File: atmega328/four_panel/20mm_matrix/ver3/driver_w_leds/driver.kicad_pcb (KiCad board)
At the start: 2 copper layers, 40 x 40 mm, 308 parts, among them IC1 ATMEGA328P-M, IC2 ATMEGA328P-M, IC3 ATMEGA328P-M, IC4 ATMEGA328P-M, P1 CONN_2X2, P2 CONN_2X2, P3 CONN_2X2, P4 CONN_2X2, X1 CER_RESO, X2 CER_RESO, X3 CER_RESO, X4 CER_RESO

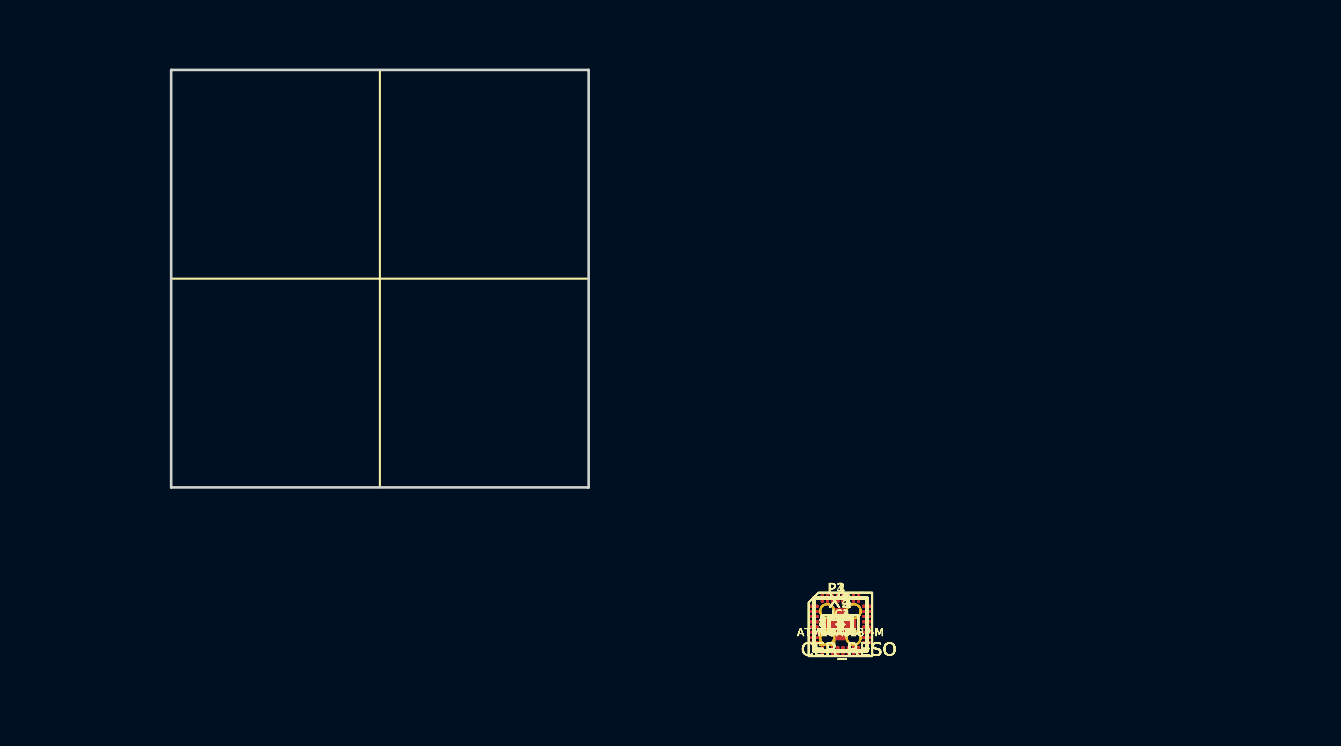
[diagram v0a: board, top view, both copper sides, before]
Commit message: Added footprint for 2x2 SMD header. Did preliminary fit test - OK but might step resistors and capacitors down to 0402 to make routing easier.
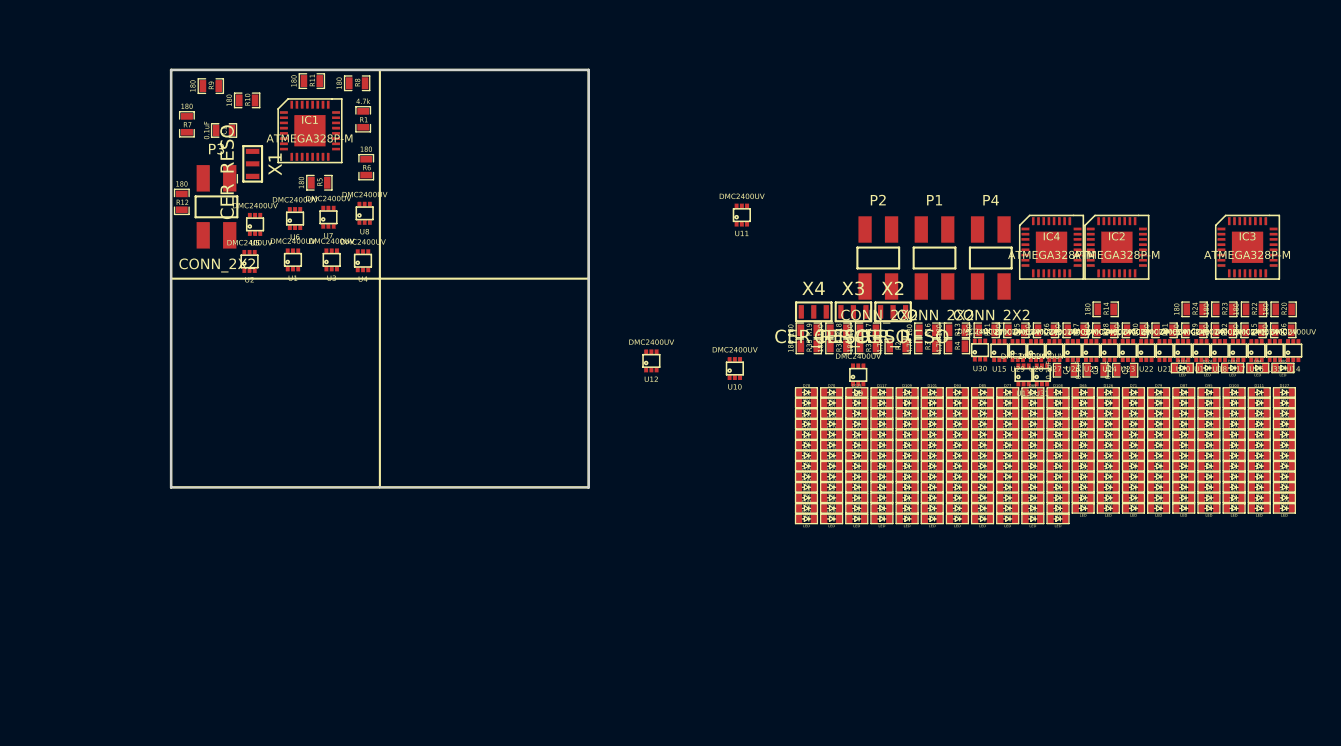
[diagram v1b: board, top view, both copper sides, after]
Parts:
- added U1: DMC2400UV, DMC2400UV, F.Cu at (61.7, 68.2)
- added U10: DMC2400UV, DMC2400UV, F.Cu at (104.0, 78.6)
- added U11: DMC2400UV, DMC2400UV, F.Cu at (104.7, 63.9)
- added U12: DMC2400UV, DMC2400UV, F.Cu at (96.0, 77.9)
- added U13: DMC2400UV, DMC2400UV, F.Cu at (131.7, 79.2)
- added U14: DMC2400UV, DMC2400UV, F.Cu at (157.5, 76.9)
- added U15: DMC2400UV, DMC2400UV, F.Cu at (129.3, 76.9)
- added U16: DMC2400UV, DMC2400UV, F.Cu at (154.0, 76.9)
- added U17: DMC2400UV, DMC2400UV, F.Cu at (152.2, 76.9)
- added U18: DMC2400UV, DMC2400UV, F.Cu at (150.5, 76.9)
- added U19: DMC2400UV, DMC2400UV, F.Cu at (148.7, 76.9)
- added U2: DMC2400UV, DMC2400UV, F.Cu at (57.5, 68.3)
- added U20: DMC2400UV, DMC2400UV, F.Cu at (146.9, 76.9)
- added U21: DMC2400UV, DMC2400UV, F.Cu at (145.2, 76.9)
- added U22: DMC2400UV, DMC2400UV, F.Cu at (143.4, 76.9)
- added U23: DMC2400UV, DMC2400UV, F.Cu at (141.7, 76.9)
- added U24: DMC2400UV, DMC2400UV, F.Cu at (139.9, 76.9)
- added U25: DMC2400UV, DMC2400UV, F.Cu at (138.2, 76.9)
- added U26: DMC2400UV, DMC2400UV, F.Cu at (136.4, 76.9)
- added U27: DMC2400UV, DMC2400UV, F.Cu at (134.6, 76.9)
- added U28: DMC2400UV, DMC2400UV, F.Cu at (132.9, 76.9)
- added U29: DMC2400UV, DMC2400UV, F.Cu at (131.1, 76.9)
- added U3: DMC2400UV, DMC2400UV, F.Cu at (65.4, 68.2)
- added U30: DMC2400UV, DMC2400UV, F.Cu at (127.5, 76.8)
- added U31: DMC2400UV, DMC2400UV, F.Cu at (133.4, 79.2)
- added U32: DMC2400UV, DMC2400UV, F.Cu at (155.8, 76.9)
- added U4: DMC2400UV, DMC2400UV, F.Cu at (68.4, 68.3)
- added U5: DMC2400UV, DMC2400UV, F.Cu at (58.0, 64.8)
- added U6: DMC2400UV, DMC2400UV, F.Cu at (61.9, 64.2)
- added U7: DMC2400UV, DMC2400UV, F.Cu at (65.1, 64.1)
- added U8: DMC2400UV, DMC2400UV, F.Cu at (68.5, 63.7)
- added U9: DMC2400UV, DMC2400UV, F.Cu at (115.8, 79.2)
- P1, P2, P3, P4: footprint PIN_ARRAY_2X2 -> SMD_2X2
- moved R9 79.4 mm to (53.8, 51.5)
- moved R7 78.8 mm to (51.5, 55.2), turned to 270 degrees
- moved R10 75.8 mm to (57.3, 52.9)
- moved C1 75.7 mm to (55.1, 55.8)
- moved R12 75.0 mm to (51.0, 62.6), turned to 270 degrees
- moved R11 72.6 mm to (63.5, 51.1)
- moved P3 71.9 mm to (54.3, 63.1)
- moved X1 71.5 mm to (57.8, 59.0), turned to 270 degrees
- moved R8 69.5 mm to (67.8, 51.3)
- moved IC1 69.4 mm to (63.3, 55.8)
- moved R1 66.6 mm to (68.4, 54.7), turned to 270 degrees
- moved R5 65.4 mm to (64.2, 60.8)
- moved R6 63.1 mm to (68.7, 59.3), turned to 270 degrees
- moved IC3 53.2 mm to (153.1, 67.0)
- moved R20 52.1 mm to (156.6, 72.9)
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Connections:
- D1 pad 2: /ROW0_DRV0 -> /ROW0_INV0
- D10 pad 2: /ROW1_DRV0 -> /ROW1_INV0
- D100 pad 2: /ROW3_DRV1 -> /ROW3_INV1
- D101 pad 2: /ROW4_DRV1 -> /ROW4_INV1
- D102 pad 2: /ROW5_DRV1 -> /ROW5_INV1
- D103 pad 2: /ROW6_DRV1 -> /ROW6_INV1
- D104 pad 2: /ROW7_DRV1 -> /ROW7_INV1
- D105 pad 2: /ROW0_DRV1 -> /ROW0_INV1
- D106 pad 2: /ROW1_DRV1 -> /ROW1_INV1
- D107 pad 2: /ROW2_DRV1 -> /ROW2_INV1
- D108 pad 2: /ROW3_DRV1 -> /ROW3_INV1
- D109 pad 2: /ROW4_DRV1 -> /ROW4_INV1
- D11 pad 2: /ROW2_DRV0 -> /ROW2_INV0
- D110 pad 2: /ROW5_DRV1 -> /ROW5_INV1
- D111 pad 2: /ROW6_DRV1 -> /ROW6_INV1
- D112 pad 2: /ROW7_DRV1 -> /ROW7_INV1
- D113 pad 2: /ROW0_DRV1 -> /ROW0_INV1
- D114 pad 2: /ROW1_DRV1 -> /ROW1_INV1
- D115 pad 2: /ROW2_DRV1 -> /ROW2_INV1
- D116 pad 2: /ROW3_DRV1 -> /ROW3_INV1
- D117 pad 2: /ROW4_DRV1 -> /ROW4_INV1
- D118 pad 2: /ROW5_DRV1 -> /ROW5_INV1
- D119 pad 2: /ROW6_DRV1 -> /ROW6_INV1
- D12 pad 2: /ROW3_DRV0 -> /ROW3_INV0
- D120 pad 2: /ROW7_DRV1 -> /ROW7_INV1
- D121 pad 2: /ROW0_DRV1 -> /ROW0_INV1
- D122 pad 2: /ROW1_DRV1 -> /ROW1_INV1
- D123 pad 2: /ROW2_DRV1 -> /ROW2_INV1
- D124 pad 2: /ROW3_DRV1 -> /ROW3_INV1
- D125 pad 2: /ROW4_DRV1 -> /ROW4_INV1
- D126 pad 2: /ROW5_DRV1 -> /ROW5_INV1
- D127 pad 2: /ROW6_DRV1 -> /ROW6_INV1
- D128 pad 2: /ROW7_DRV1 -> /ROW7_INV1
- D129 pad 2: /ROW0_DRV2 -> /ROW0_INV2
- D13 pad 2: /ROW4_DRV0 -> /ROW4_INV0
- D130 pad 2: /ROW1_DRV2 -> /ROW1_INV2
- D131 pad 2: /ROW2_DRV2 -> /ROW2_INV2
- D132 pad 2: /ROW3_DRV2 -> /ROW3_INV2
- D133 pad 2: /ROW4_DRV2 -> /ROW4_INV2
- D134 pad 2: /ROW5_DRV2 -> /ROW5_INV2
- D135 pad 2: /ROW6_DRV2 -> /ROW6_INV2
- D136 pad 2: /ROW7_DRV2 -> /ROW7_INV2
- D137 pad 2: /ROW0_DRV2 -> /ROW0_INV2
- D138 pad 2: /ROW1_DRV2 -> /ROW1_INV2
- D139 pad 2: /ROW2_DRV2 -> /ROW2_INV2
- D14 pad 2: /ROW5_DRV0 -> /ROW5_INV0
- D140 pad 2: /ROW3_DRV2 -> /ROW3_INV2
- D141 pad 2: /ROW4_DRV2 -> /ROW4_INV2
- D142 pad 2: /ROW5_DRV2 -> /ROW5_INV2
- D143 pad 2: /ROW6_DRV2 -> /ROW6_INV2
- D144 pad 2: /ROW7_DRV2 -> /ROW7_INV2
- D145 pad 2: /ROW0_DRV2 -> /ROW0_INV2
- D146 pad 2: /ROW1_DRV2 -> /ROW1_INV2
- D147 pad 2: /ROW2_DRV2 -> /ROW2_INV2
- D148 pad 2: /ROW3_DRV2 -> /ROW3_INV2
- D149 pad 2: /ROW4_DRV2 -> /ROW4_INV2
- D15 pad 2: /ROW6_DRV0 -> /ROW6_INV0
- D150 pad 2: /ROW5_DRV2 -> /ROW5_INV2
- D151 pad 2: /ROW6_DRV2 -> /ROW6_INV2
- D152 pad 2: /ROW7_DRV2 -> /ROW7_INV2
- D153 pad 2: /ROW0_DRV2 -> /ROW0_INV2
- D154 pad 2: /ROW1_DRV2 -> /ROW1_INV2
- D155 pad 2: /ROW2_DRV2 -> /ROW2_INV2
- D156 pad 2: /ROW3_DRV2 -> /ROW3_INV2
- D157 pad 2: /ROW4_DRV2 -> /ROW4_INV2
- D158 pad 2: /ROW5_DRV2 -> /ROW5_INV2
- D159 pad 2: /ROW6_DRV2 -> /ROW6_INV2
- D16 pad 2: /ROW7_DRV0 -> /ROW7_INV0
- D160 pad 2: /ROW7_DRV2 -> /ROW7_INV2
- D161 pad 2: /ROW0_DRV2 -> /ROW0_INV2
- D162 pad 2: /ROW1_DRV2 -> /ROW1_INV2
- D163 pad 2: /ROW2_DRV2 -> /ROW2_INV2
- D164 pad 2: /ROW3_DRV2 -> /ROW3_INV2
- D165 pad 2: /ROW4_DRV2 -> /ROW4_INV2
- D166 pad 2: /ROW5_DRV2 -> /ROW5_INV2
- D167 pad 2: /ROW6_DRV2 -> /ROW6_INV2
- D168 pad 2: /ROW7_DRV2 -> /ROW7_INV2
- D169 pad 2: /ROW0_DRV2 -> /ROW0_INV2
- D17 pad 2: /ROW0_DRV0 -> /ROW0_INV0
- D170 pad 2: /ROW1_DRV2 -> /ROW1_INV2
- D171 pad 2: /ROW2_DRV2 -> /ROW2_INV2
- D172 pad 2: /ROW3_DRV2 -> /ROW3_INV2
- D173 pad 2: /ROW4_DRV2 -> /ROW4_INV2
- D174 pad 2: /ROW5_DRV2 -> /ROW5_INV2
- D175 pad 2: /ROW6_DRV2 -> /ROW6_INV2
- D176 pad 2: /ROW7_DRV2 -> /ROW7_INV2
- D177 pad 2: /ROW0_DRV2 -> /ROW0_INV2
- D178 pad 2: /ROW1_DRV2 -> /ROW1_INV2
- D179 pad 2: /ROW2_DRV2 -> /ROW2_INV2
- D18 pad 2: /ROW1_DRV0 -> /ROW1_INV0
- D180 pad 2: /ROW3_DRV2 -> /ROW3_INV2
- D181 pad 2: /ROW4_DRV2 -> /ROW4_INV2
- D182 pad 2: /ROW5_DRV2 -> /ROW5_INV2
- D183 pad 2: /ROW6_DRV2 -> /ROW6_INV2
- D184 pad 2: /ROW7_DRV2 -> /ROW7_INV2
- D185 pad 2: /ROW0_DRV2 -> /ROW0_INV2
- D186 pad 2: /ROW1_DRV2 -> /ROW1_INV2
- D187 pad 2: /ROW2_DRV2 -> /ROW2_INV2
- D188 pad 2: /ROW3_DRV2 -> /ROW3_INV2
- D189 pad 2: /ROW4_DRV2 -> /ROW4_INV2
- D19 pad 2: /ROW2_DRV0 -> /ROW2_INV0
- D190 pad 2: /ROW5_DRV2 -> /ROW5_INV2
- D191 pad 2: /ROW6_DRV2 -> /ROW6_INV2
- D192 pad 2: /ROW7_DRV2 -> /ROW7_INV2
- D193 pad 2: /ROW0_DRV3 -> /ROW0_INV3
- D194 pad 2: /ROW1_DRV3 -> /ROW1_INV3
- D195 pad 2: /ROW2_DRV3 -> /ROW2_INV3
- D196 pad 2: /ROW3_DRV3 -> /ROW3_INV3
- D197 pad 2: /ROW4_DRV3 -> /ROW4_INV3
- D198 pad 2: /ROW5_DRV3 -> /ROW5_INV3
- D199 pad 2: /ROW6_DRV3 -> /ROW6_INV3
- D2 pad 2: /ROW1_DRV0 -> /ROW1_INV0
- D20 pad 2: /ROW3_DRV0 -> /ROW3_INV0
- D200 pad 2: /ROW7_DRV3 -> /ROW7_INV3
- D201 pad 2: /ROW0_DRV3 -> /ROW0_INV3
- D202 pad 2: /ROW1_DRV3 -> /ROW1_INV3
- D203 pad 2: /ROW2_DRV3 -> /ROW2_INV3
- D204 pad 2: /ROW3_DRV3 -> /ROW3_INV3
- D205 pad 2: /ROW4_DRV3 -> /ROW4_INV3
- D206 pad 2: /ROW5_DRV3 -> /ROW5_INV3
- D207 pad 2: /ROW6_DRV3 -> /ROW6_INV3
- D208 pad 2: /ROW7_DRV3 -> /ROW7_INV3
- D209 pad 2: /ROW0_DRV3 -> /ROW0_INV3
- D21 pad 2: /ROW4_DRV0 -> /ROW4_INV0
- D210 pad 2: /ROW1_DRV3 -> /ROW1_INV3
- D211 pad 2: /ROW2_DRV3 -> /ROW2_INV3
- D212 pad 2: /ROW3_DRV3 -> /ROW3_INV3
- D213 pad 2: /ROW4_DRV3 -> /ROW4_INV3
- D214 pad 2: /ROW5_DRV3 -> /ROW5_INV3
- D215 pad 2: /ROW6_DRV3 -> /ROW6_INV3
- D216 pad 2: /ROW7_DRV3 -> /ROW7_INV3
- D217 pad 2: /ROW0_DRV3 -> /ROW0_INV3
- D218 pad 2: /ROW1_DRV3 -> /ROW1_INV3
- D219 pad 2: /ROW2_DRV3 -> /ROW2_INV3
- D22 pad 2: /ROW5_DRV0 -> /ROW5_INV0
- D220 pad 2: /ROW3_DRV3 -> /ROW3_INV3
- D221 pad 2: /ROW4_DRV3 -> /ROW4_INV3
- D222 pad 2: /ROW5_DRV3 -> /ROW5_INV3
- D223 pad 2: /ROW6_DRV3 -> /ROW6_INV3
- D224 pad 2: /ROW7_DRV3 -> /ROW7_INV3
- D225 pad 2: /ROW0_DRV3 -> /ROW0_INV3
- D226 pad 2: /ROW1_DRV3 -> /ROW1_INV3
- D227 pad 2: /ROW2_DRV3 -> /ROW2_INV3
- D228 pad 2: /ROW3_DRV3 -> /ROW3_INV3
- D229 pad 2: /ROW4_DRV3 -> /ROW4_INV3
- D23 pad 2: /ROW6_DRV0 -> /ROW6_INV0
- D230 pad 2: /ROW5_DRV3 -> /ROW5_INV3
- D231 pad 2: /ROW6_DRV3 -> /ROW6_INV3
- D232 pad 2: /ROW7_DRV3 -> /ROW7_INV3
- D233 pad 2: /ROW0_DRV3 -> /ROW0_INV3
- D234 pad 2: /ROW1_DRV3 -> /ROW1_INV3
- D235 pad 2: /ROW2_DRV3 -> /ROW2_INV3
- D236 pad 2: /ROW3_DRV3 -> /ROW3_INV3
- D237 pad 2: /ROW4_DRV3 -> /ROW4_INV3
- D238 pad 2: /ROW5_DRV3 -> /ROW5_INV3
- D239 pad 2: /ROW6_DRV3 -> /ROW6_INV3
- D24 pad 2: /ROW7_DRV0 -> /ROW7_INV0
- D240 pad 2: /ROW7_DRV3 -> /ROW7_INV3
- D241 pad 2: /ROW0_DRV3 -> /ROW0_INV3
- D242 pad 2: /ROW1_DRV3 -> /ROW1_INV3
- D243 pad 2: /ROW2_DRV3 -> /ROW2_INV3
- D244 pad 2: /ROW3_DRV3 -> /ROW3_INV3
- D245 pad 2: /ROW4_DRV3 -> /ROW4_INV3
- D246 pad 2: /ROW5_DRV3 -> /ROW5_INV3
- D247 pad 2: /ROW6_DRV3 -> /ROW6_INV3
- D248 pad 2: /ROW7_DRV3 -> /ROW7_INV3
- D249 pad 2: /ROW0_DRV3 -> /ROW0_INV3
- D25 pad 2: /ROW0_DRV0 -> /ROW0_INV0
- D250 pad 2: /ROW1_DRV3 -> /ROW1_INV3
- D251 pad 2: /ROW2_DRV3 -> /ROW2_INV3
- D252 pad 2: /ROW3_DRV3 -> /ROW3_INV3
- D253 pad 2: /ROW4_DRV3 -> /ROW4_INV3
- D254 pad 2: /ROW5_DRV3 -> /ROW5_INV3
- D255 pad 2: /ROW6_DRV3 -> /ROW6_INV3
- D256 pad 2: /ROW7_DRV3 -> /ROW7_INV3
- D26 pad 2: /ROW1_DRV0 -> /ROW1_INV0
- D27 pad 2: /ROW2_DRV0 -> /ROW2_INV0
- D28 pad 2: /ROW3_DRV0 -> /ROW3_INV0
- D29 pad 2: /ROW4_DRV0 -> /ROW4_INV0
- D3 pad 2: /ROW2_DRV0 -> /ROW2_INV0
- D30 pad 2: /ROW5_DRV0 -> /ROW5_INV0
- D31 pad 2: /ROW6_DRV0 -> /ROW6_INV0
- D32 pad 2: /ROW7_DRV0 -> /ROW7_INV0
- D33 pad 2: /ROW0_DRV0 -> /ROW0_INV0
- D34 pad 2: /ROW1_DRV0 -> /ROW1_INV0
- D35 pad 2: /ROW2_DRV0 -> /ROW2_INV0
- D36 pad 2: /ROW3_DRV0 -> /ROW3_INV0
- D37 pad 2: /ROW4_DRV0 -> /ROW4_INV0
- D38 pad 2: /ROW5_DRV0 -> /ROW5_INV0
- D39 pad 2: /ROW6_DRV0 -> /ROW6_INV0
- D4 pad 2: /ROW3_DRV0 -> /ROW3_INV0
- D40 pad 2: /ROW7_DRV0 -> /ROW7_INV0
- D41 pad 2: /ROW0_DRV0 -> /ROW0_INV0
- D42 pad 2: /ROW1_DRV0 -> /ROW1_INV0
- D43 pad 2: /ROW2_DRV0 -> /ROW2_INV0
- D44 pad 2: /ROW3_DRV0 -> /ROW3_INV0
- D45 pad 2: /ROW4_DRV0 -> /ROW4_INV0
- D46 pad 2: /ROW5_DRV0 -> /ROW5_INV0
- D47 pad 2: /ROW6_DRV0 -> /ROW6_INV0
- D48 pad 2: /ROW7_DRV0 -> /ROW7_INV0
- D49 pad 2: /ROW0_DRV0 -> /ROW0_INV0
- D5 pad 2: /ROW4_DRV0 -> /ROW4_INV0
- D50 pad 2: /ROW1_DRV0 -> /ROW1_INV0
- D51 pad 2: /ROW2_DRV0 -> /ROW2_INV0
- D52 pad 2: /ROW3_DRV0 -> /ROW3_INV0
- D53 pad 2: /ROW4_DRV0 -> /ROW4_INV0
- D54 pad 2: /ROW5_DRV0 -> /ROW5_INV0
- D55 pad 2: /ROW6_DRV0 -> /ROW6_INV0
- D56 pad 2: /ROW7_DRV0 -> /ROW7_INV0
- D57 pad 2: /ROW0_DRV0 -> /ROW0_INV0
- D58 pad 2: /ROW1_DRV0 -> /ROW1_INV0
- D59 pad 2: /ROW2_DRV0 -> /ROW2_INV0
- D6 pad 2: /ROW5_DRV0 -> /ROW5_INV0
- D60 pad 2: /ROW3_DRV0 -> /ROW3_INV0
- D61 pad 2: /ROW4_DRV0 -> /ROW4_INV0
- D62 pad 2: /ROW5_DRV0 -> /ROW5_INV0
- D63 pad 2: /ROW6_DRV0 -> /ROW6_INV0
- D64 pad 2: /ROW7_DRV0 -> /ROW7_INV0
- D65 pad 2: /ROW0_DRV1 -> /ROW0_INV1
- D66 pad 2: /ROW1_DRV1 -> /ROW1_INV1
- D67 pad 2: /ROW2_DRV1 -> /ROW2_INV1
- D68 pad 2: /ROW3_DRV1 -> /ROW3_INV1
- D69 pad 2: /ROW4_DRV1 -> /ROW4_INV1
- D7 pad 2: /ROW6_DRV0 -> /ROW6_INV0
- D70 pad 2: /ROW5_DRV1 -> /ROW5_INV1
- D71 pad 2: /ROW6_DRV1 -> /ROW6_INV1
- D72 pad 2: /ROW7_DRV1 -> /ROW7_INV1
- D73 pad 2: /ROW0_DRV1 -> /ROW0_INV1
- D74 pad 2: /ROW1_DRV1 -> /ROW1_INV1
- D75 pad 2: /ROW2_DRV1 -> /ROW2_INV1
- D76 pad 2: /ROW3_DRV1 -> /ROW3_INV1
- D77 pad 2: /ROW4_DRV1 -> /ROW4_INV1
- D78 pad 2: /ROW5_DRV1 -> /ROW5_INV1
- D79 pad 2: /ROW6_DRV1 -> /ROW6_INV1
- D8 pad 2: /ROW7_DRV0 -> /ROW7_INV0
- D80 pad 2: /ROW7_DRV1 -> /ROW7_INV1
- D81 pad 2: /ROW0_DRV1 -> /ROW0_INV1
- D82 pad 2: /ROW1_DRV1 -> /ROW1_INV1
- D83 pad 2: /ROW2_DRV1 -> /ROW2_INV1
- D84 pad 2: /ROW3_DRV1 -> /ROW3_INV1
- D85 pad 2: /ROW4_DRV1 -> /ROW4_INV1
- D86 pad 2: /ROW5_DRV1 -> /ROW5_INV1
- D87 pad 2: /ROW6_DRV1 -> /ROW6_INV1
- D88 pad 2: /ROW7_DRV1 -> /ROW7_INV1
- D89 pad 2: /ROW0_DRV1 -> /ROW0_INV1
- D9 pad 2: /ROW0_DRV0 -> /ROW0_INV0
- D90 pad 2: /ROW1_DRV1 -> /ROW1_INV1
- D91 pad 2: /ROW2_DRV1 -> /ROW2_INV1
- D92 pad 2: /ROW3_DRV1 -> /ROW3_INV1
- D93 pad 2: /ROW4_DRV1 -> /ROW4_INV1
- D94 pad 2: /ROW5_DRV1 -> /ROW5_INV1
- D95 pad 2: /ROW6_DRV1 -> /ROW6_INV1
- D96 pad 2: /ROW7_DRV1 -> /ROW7_INV1
- D97 pad 2: /ROW0_DRV1 -> /ROW0_INV1
- D98 pad 2: /ROW1_DRV1 -> /ROW1_INV1
- D99 pad 2: /ROW2_DRV1 -> /ROW2_INV1

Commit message: Finished preliminary component layout for driver with leds.
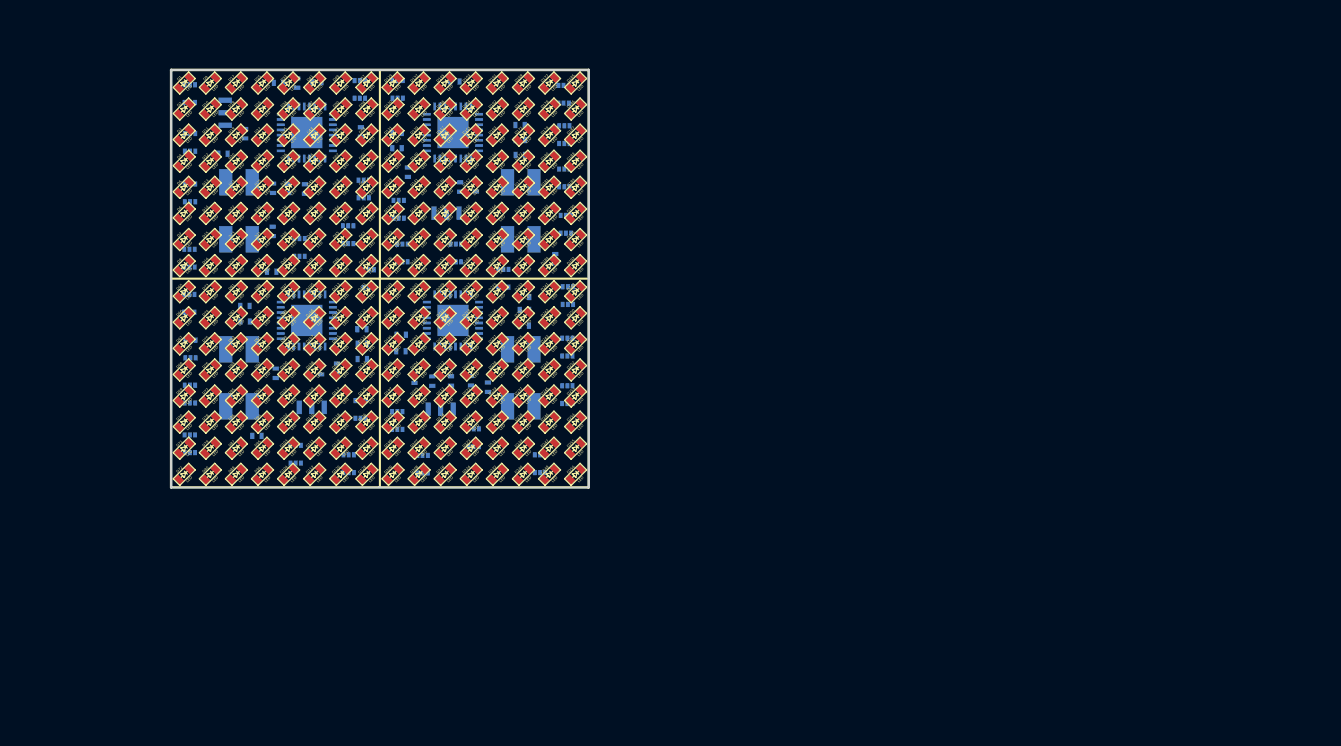
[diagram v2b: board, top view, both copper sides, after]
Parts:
- C1, C2, C3, C4: footprint SM0603_Capa -> SM0402; moved to B.Cu
- IC1, IC2, IC3, IC4, P1, P2, P3, P4, U1, U10, U11, U12, U13, U14, U15, U16, U17, U18, U19, U2, U20, U21, U22, U23, U24, U25, U26, U27, U28, U29, U3, U30, U31, U32, U4, U5, U6, U7, U8, U9, X1, X2, X3, X4: moved to B.Cu
- R1, R10, R11, R12, R13, R14, R15, R16, R17, R18, R19, R2, R20, R21, R22, R23, R24, R25, R26, R27, R28, R29, R3, R30, R31, R32, R33, R34, R35, R36, R4, R5, R6, R7, R8, R9: footprint SM0603_Resistor -> SM0402; moved to B.Cu
- moved U14 106.1 mm to (51.8, 85.8)
- moved D75 103.4 mm to (53.8, 76.2), turned to 45 degrees
- moved D2 102.1 mm to (51.2, 53.8), turned to 45 degrees
- moved D10 102.1 mm to (53.8, 53.8), turned to 45 degrees
- moved D18 102.0 mm to (56.2, 53.8), turned to 45 degrees
- moved D26 101.9 mm to (58.8, 53.8), turned to 45 degrees
- moved D6 101.6 mm to (51.2, 63.8), turned to 45 degrees
- moved D14 101.5 mm to (53.8, 63.8), turned to 45 degrees
- moved D22 101.5 mm to (56.2, 63.8), turned to 45 degrees
- moved D30 101.4 mm to (58.8, 63.8), turned to 45 degrees
- moved D86 100.4 mm to (56.2, 83.8), turned to 45 degrees
- moved R20 99.5 mm to (57.1, 72.6), turned to 180 degrees
- moved D83 98.5 mm to (56.2, 76.2), turned to 45 degrees
- moved D94 95.5 mm to (58.8, 83.8), turned to 45 degrees
- moved D91 93.6 mm to (58.8, 76.2), turned to 45 degrees
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
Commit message: Minor changes to schematic.
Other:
- rule via_min_drill: 0.508 -> 0.381
- rule via_min_size: 0.762 -> 0.508
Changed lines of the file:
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@@
     (links 785)
     (no_connects 785)
-    (area 49.874999 49.874999 162.6886 108.224361)
+    (area 49.874999 49.874999 90.125001 90.125001)
     (thickness 1.6)
     (drawings 8)
@@
     (via_size 0.762)
     (via_drill 0.508)
-    (via_min_size 0.762)
-    (via_min_drill 0.508)
+    (via_min_size 0.508)
+    (via_min_drill 0.381)
     (uvia_size 0.508)
     (uvia_drill 0.127)

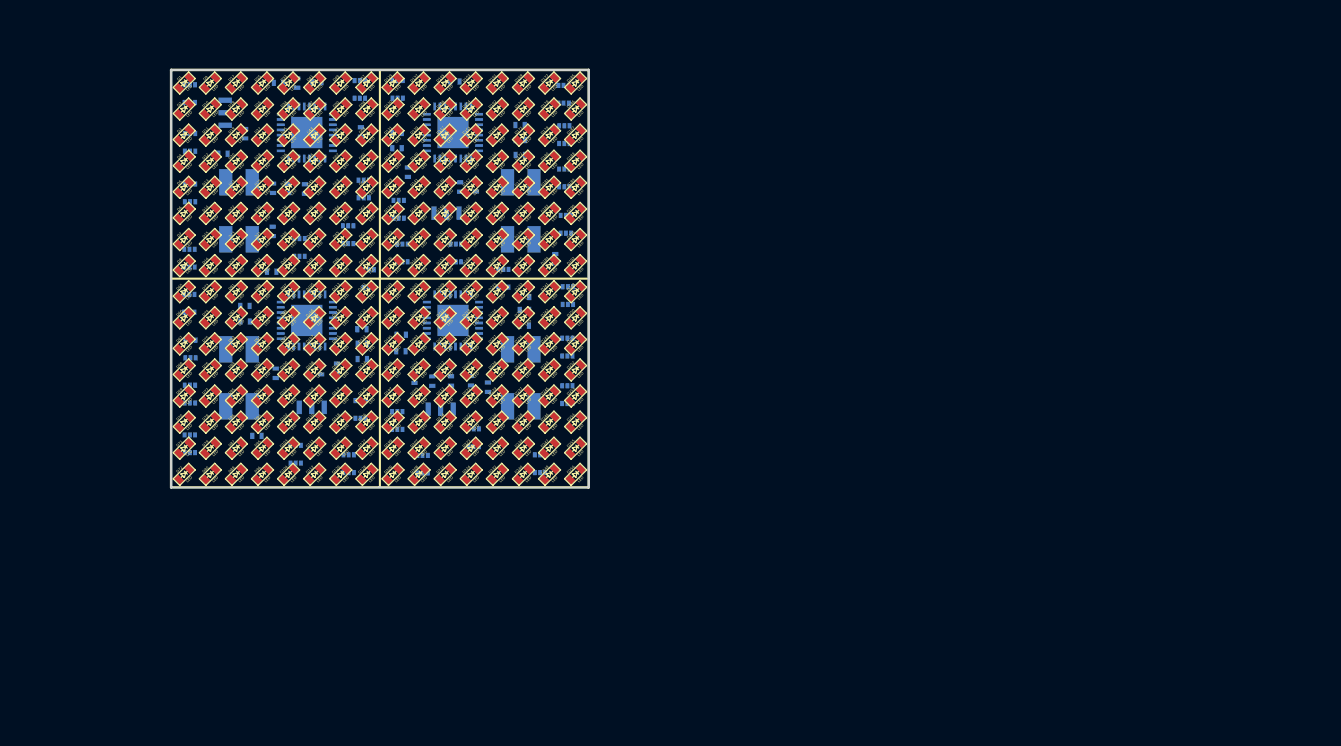
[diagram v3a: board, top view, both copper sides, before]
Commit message: More work on layout for driver w leds.
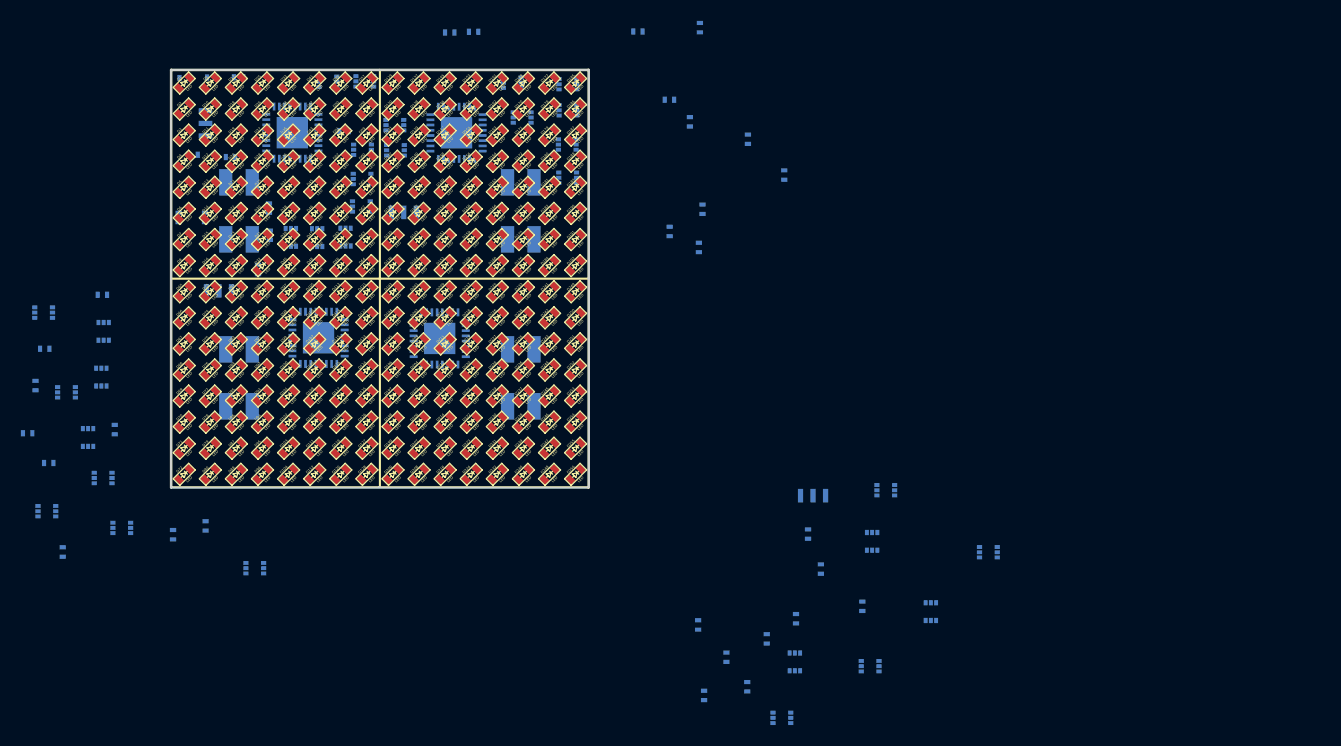
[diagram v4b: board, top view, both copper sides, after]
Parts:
- moved R34 48.2 mm to (116.2, 101.4)
- moved R36 47.3 mm to (105.2, 109.1), turned to 270 degrees
- moved U29 46.9 mm to (117.2, 95.2), turned to 180 degrees
- moved U25 46.1 mm to (122.8, 101.9)
- moved R35 43.9 mm to (101.1, 109.9), turned to 270 degrees
- moved U30 43.8 mm to (117.0, 107.1), turned to 270 degrees
- moved U28 43.1 mm to (128.3, 96.2), turned to 270 degrees
- moved U26 41.9 mm to (118.5, 90.3), turned to 270 degrees
- moved C4 41.6 mm to (109.9, 102.6)
- moved R30 39.1 mm to (107.1, 104.5), turned to 270 degrees
- moved R33 37.2 mm to (111.0, 94.5)
- moved U27 37.2 mm to (109.8, 106.7), turned to 180 degrees
- moved R31 36.8 mm to (112.2, 97.8), turned to 270 degrees
- moved X4 36.6 mm to (111.5, 90.8)
- moved R32 36.1 mm to (103.2, 106.3)
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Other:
- copper layers 2 -> 4
- net class Default: via_dia 0.762 -> 0.508; via_drill 0.508 -> 0.381
